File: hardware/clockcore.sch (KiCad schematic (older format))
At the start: 59 parts, among them J1 Header, J2 Ext, J3 JTAG, J7 GCT_USB4108-GF-A, Q1 MBT3904DW1T1G, SW1 Reset, SW2 Boot, U1 AP2114H-3_3TRG1, U2 ‎SN74HCT245PWR‎, U3 ESP32-WROOM-32, U4 DS1338Z-33+, U5 FT231XS, U6 USBLC6-4SC6, Y1 32.768Hz, 12.5pF, 45kΩ

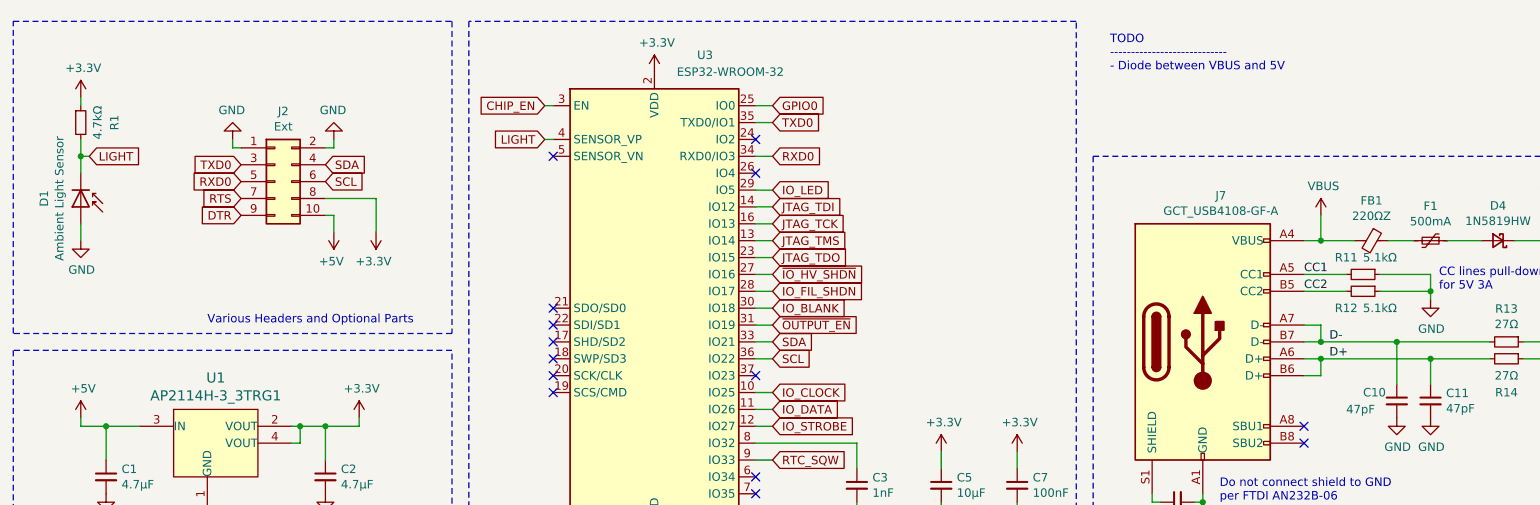
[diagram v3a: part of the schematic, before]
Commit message: add ds18b20 to clock core and reroute a few traces
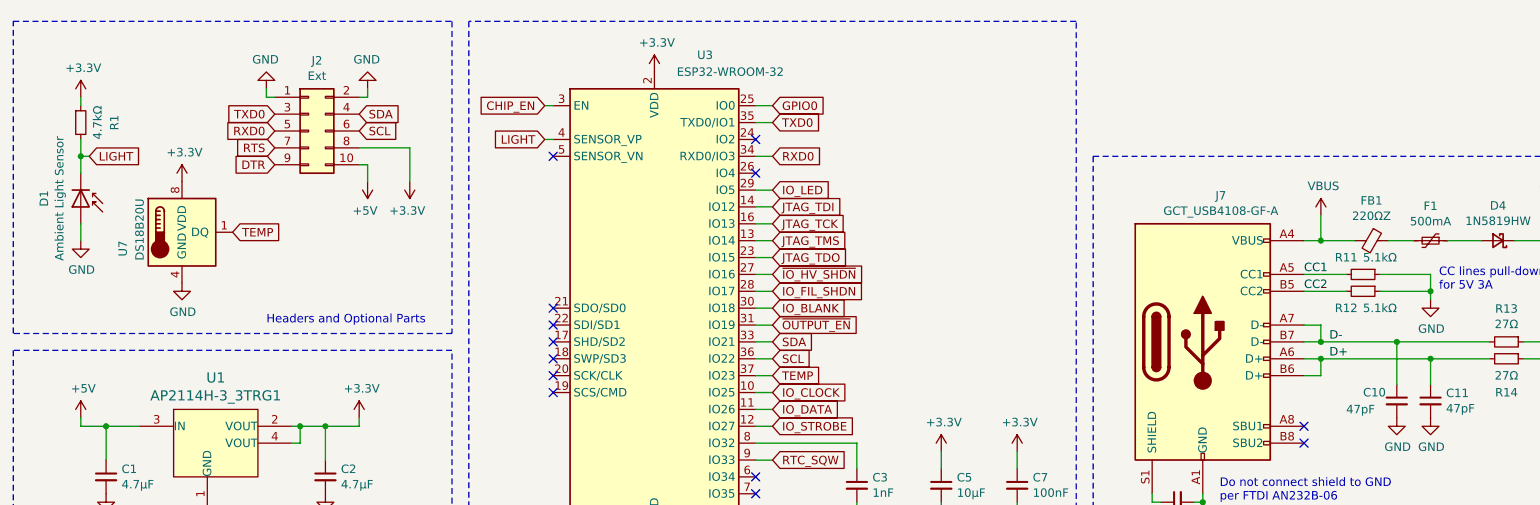
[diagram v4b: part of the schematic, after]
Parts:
- added U7: DS18B20U, Package_SO:MSOP-8_3x3mm_P0.65mm, symbol Sensor_Temperature:DS18B20U
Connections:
- net +3V3: now also U7.8 (VDD)
- net GND: now also U7.4 (GND)
- net TEMP: now reaches U3.37 (IO23)
- net TEMP: now also U7.1 (DQ)
- no-connect marks 27 -> 26
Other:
- note added: "Headers and Optional Parts"
- note removed: "TODO\n----------------------------\n- Diode between VBUS and 5V"
- note removed: "Various Headers and Optional Parts"
- moved on the sheet: J2
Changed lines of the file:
@@
 encoding utf-8
 Sheet 1 1
-Title ""
-Date ""
-Rev "1"
+Title "Clock Core"
+Date "2020-08-02"
+Rev "1.0"
 Comp ""
 Comment1 "Designed for AISLER 2-Layer Service"
-Comment2 ""
-Comment3 ""
+Comment2 "Made for IVL2-7/5 VFD Driver Board"
+Comment3 "ESP32 + RTC"
 Comment4 ""
 $EndDescr
@@
 L power:GND #PWR03
 U 1 1 5F700789
-P 2450 1300
-F 0 "#PWR03" H 2450 1050 50  0001 C CNN
-F 1 "GND" H 2455 1127 50  0000 C CNN
-F 2 "" H 2450 1300 50  0001 C CNN
-F 3 "" H 2450 1300 50  0001 C CNN
-	1    2450 1300
+P 2650 1000
+F 0 "#PWR03" H 2650 750 50  0001 C CNN
+F 1 "GND" H 2655 827 50  0000 C CNN
+F 2 "" H 2650 1000 50  0001 C CNN
+F 3 "" H 2650 1000 50  0001 C CNN
+	1    2650 1000
 	-1   0    0    1
 $EndComp
@@
 L power:GND #PWR010
 U 1 1 5F700DB1
-P 1850 1300
-F 0 "#PWR010" H 1850 1050 50  0001 C CNN
-F 1 "GND" H 1855 1127 50  0000 C CNN
-F 2 "" H 1850 1300 50  0001 C CNN
-F 3 "" H 1850 1300 50  0001 C CNN
-	1    1850 1300
+P 2050 1000
+F 0 "#PWR010" H 2050 750 50  0001 C CNN
+F 1 "GND" H 2055 827 50  0000 C CNN
+F 2 "" H 2050 1000 50  0001 C CNN
+F 3 "" H 2050 1000 50  0001 C CNN
+	1    2050 1000
 	-1   0    0    1
 $EndComp
@@
 L power:+3.3V #PWR02
 U 1 1 5F713013
-P 2700 1850
-F 0 "#PWR02" H 2700 1700 50  0001 C CNN
-F 1 "+3.3V" H 2715 2023 50  0000 C CNN
-F 2 "" H 2700 1850 50  0001 C CNN
-F 3 "" H 2700 1850 50  0001 C CNN
-	1    2700 1850
+P 2900 1550
+F 0 "#PWR02" H 2900 1400 50  0001 C CNN
+F 1 "+3.3V" H 2915 1723 50  0000 C CNN
+F 2 "" H 2900 1550 50  0001 C CNN
+F 3 "" H 2900 1550 50  0001 C CNN
+	1    2900 1550
 	-1   0    0    1
 $EndComp
@@
 L power:+5V #PWR08
 U 1 1 5F713FBF
-P 2450 1850
-F 0 "#PWR08" H 2450 1700 50  0001 C CNN
-F 1 "+5V" H 2465 2023 50  0000 C CNN
-F 2 "" H 2450 1850 50  0001 C CNN
-F 3 "" H 2450 1850 50  0001 C CNN
-	1    2450 1850
+P 2650 1550
+F 0 "#PWR08" H 2650 1400 50  0001 C CNN
+F 1 "+5V" H 2665 1723 50  0000 C CNN
+F 2 "" H 2650 1550 50  0001 C CNN
+F 3 "" H 2650 1550 50  0001 C CNN
+	1    2650 1550
 	-1   0    0    1
 $EndComp
-Text GLabel 2400 1450 2    50   Input ~ 0
+Text GLabel 2600 1150 2    50   Input ~ 0
 SDA
-Text GLabel 2400 1550 2    50   Input ~ 0
+Text GLabel 2600 1250 2    50   Input ~ 0
 SCL
-Text GLabel 1900 1450 0    50   Input ~ 0
+Text GLabel 2100 1150 0    50   Input ~ 0
 TXD0
-Text GLabel 1900 1550 0    50   Input ~ 0
+Text GLabel 2100 1250 0    50   Input ~ 0
 RXD0
-Text GLabel 1900 1650 0    50   Input ~ 0
+Text GLabel 2100 1350 0    50   Input ~ 0
 RTS
-Text GLabel 1900 1750 0    50   Input ~ 0
+Text GLabel 2100 1450 0    50   Input ~ 0
 DTR
 $Comp
@@
 Wire Notes Line
 	3150 2450 550  2450
-Text Notes 1700 2400 0    50   ~ 0
-Various Headers and Optional Parts
+Text Notes 2050 2400 0    50   ~ 0
+Headers and Optional Parts
 Text GLabel 5050 1100 2    50   Input ~ 0
 GPIO0
@@
 Wire Wire Line
 	4950 2400 5050 2400
-NoConn ~ 4950 2700
 Wire Notes Line
 	3250 600  3250 4000
@@
 NoConn ~ 1200 5350
 Wire Wire Line
-	2450 1300 2450 1350
-Wire Wire Line
-	2450 1350 2400 1350
-Wire Wire Line
-	1900 1350 1850 1350
-Wire Wire Line
-	1850 1350 1850 1300
-Wire Wire Line
-	2400 1750 2450 1750
-Wire Wire Line
-	2450 1750 2450 1850
-Wire Wire Line
-	2400 1650 2700 1650
-Wire Wire Line
-	2700 1650 2700 1850
+	2650 1000 2650 1050
+Wire Wire Line
+	2650 1050 2600 1050
+Wire Wire Line
+	2100 1050 2050 1050
+Wire Wire Line
+	2050 1050 2050 1000
+Wire Wire Line
+	2600 1450 2650 1450
+Wire Wire Line
+	2650 1450 2650 1550
+Wire Wire Line
+	2600 1350 2900 1350
+Wire Wire Line
+	2900 1350 2900 1550
 $Comp
 L Connector_Generic:Conn_02x05_Odd_Even J2
 U 1 1 5F5E992B
-P 2100 1550
-F 0 "J2" H 2150 1967 50  0000 C CNN
-F 1 "Ext" H 2150 1876 50  0000 C CNN
-F 2 "Connector_PinHeader_2.54mm:PinHeader_2x05_P2.54mm_Vertical" H 2100 1550 50  0001 C CNN
-F 3 "~" H 2100 1550 50  0001 C CNN
-	1    2100 1550
+P 2300 1250
+F 0 "J2" H 2350 1667 50  0000 C CNN
+F 1 "Ext" H 2350 1576 50  0000 C CNN
+F 2 "Connector_PinHeader_2.54mm:PinHeader_2x05_P2.54mm_Vertical" H 2300 1250 50  0001 C CNN
+F 3 "~" H 2300 1250 50  0001 C CNN
+	1    2300 1250
 	1    0    0    -1
 $EndComp
@@
 	1    0    0    -1
 $EndComp
-Text Notes 7050 900  0    50   ~ 0
-TODO\n----------------------------\n- Diode between VBUS and 5V
 Wire Wire Line
 	8500 1900 8300 1900
@@
 Wire Wire Line
 	9450 1900 9650 1900
+$Comp
+L Sensor_Temperature:DS18B20U U7
+U 1 1 5F27C2CD
+P 1550 1850
+F 0 "U7" V 1200 1800 50  0000 R CNN
+F 1 "DS18B20U" V 1300 2050 50  0000 R CNN
+F 2 "Package_SO:MSOP-8_3x3mm_P0.65mm" H 600 1600 50  0001 C CNN
+F 3 "http://datasheets.maximintegrated.com/en/ds/DS18B20.pdf" H 1400 2100 50  0001 C CNN
+	1    1550 1850
+	1    0    0    -1
+$EndComp
+$Comp
+L power:+3.3V #PWR0101
+U 1 1 5F27DD47
+P 1550 1550
+F 0 "#PWR0101" H 1550 1400 50  0001 C CNN
+F 1 "+3.3V" H 1565 1723 50  0000 C CNN
+F 2 "" H 1550 1550 50  0001 C CNN
+F 3 "" H 1550 1550 50  0001 C CNN
+	1    1550 1550
+	1    0    0    -1
+$EndComp
+$Comp
+L power:GND #PWR0102
+U 1 1 5F27E074
+P 1550 2150
+F 0 "#PWR0102" H 1550 1900 50  0001 C CNN
+F 1 "GND" H 1555 1977 50  0000 C CNN
+F 2 "" H 1550 2150 50  0001 C CNN
+F 3 "" H 1550 2150 50  0001 C CNN
+	1    1550 2150
+	1    0    0    -1
+$EndComp
+Text GLabel 1850 1850 2    50   Input ~ 0
+TEMP
+Text GLabel 5050 2700 2    50   Input ~ 0
+TEMP
+Wire Wire Line
+	4950 2700 5050 2700
 $EndSCHEMATC

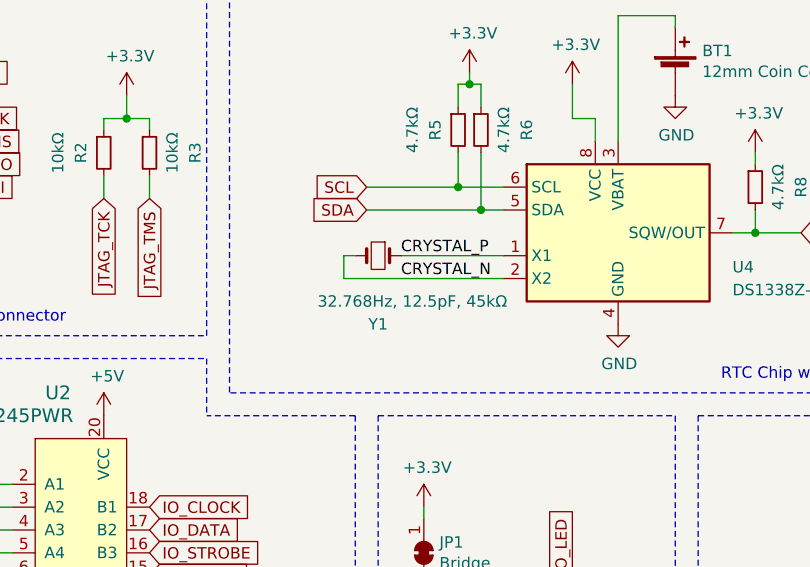
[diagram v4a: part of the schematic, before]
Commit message: updated crystal in schematic so pin3 is gnd, added teardrops
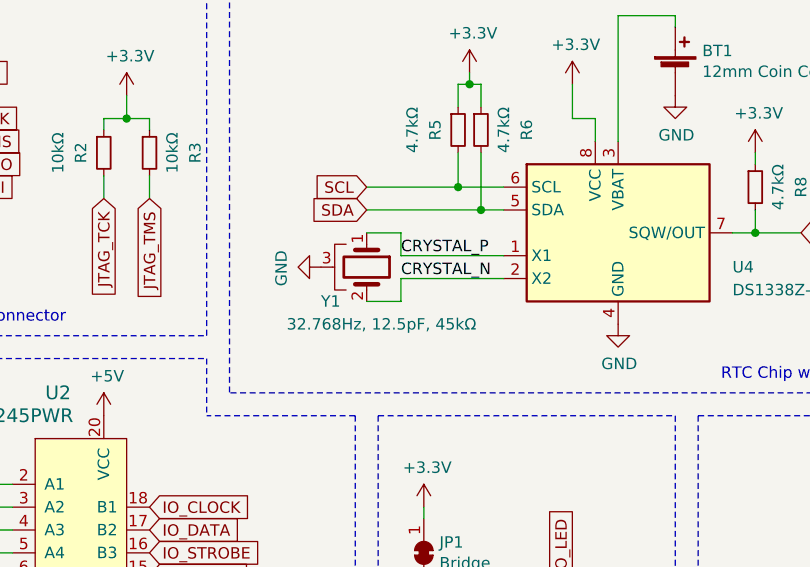
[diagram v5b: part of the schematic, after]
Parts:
- removed Y1: 32.768Hz, 12.5pF, 45kΩ, Crystal:Crystal_SMD_MicroCrystal_MS1V-T1K, symbol Device:Crystal_Small
- added Y1: 32.768Hz, 12.5pF, 45kΩ, Crystal:Crystal_SMD_MicroCrystal_MS1V-T1K, symbol Device:Crystal_GND3
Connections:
- net CRYSTAL_N: now also Y1.2
- net CRYSTAL_P: now also Y1.1
- net GND: now also Y1.3
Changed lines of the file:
@@
 Text GLabel 3850 4950 0    50   Input ~ 0
 SCL
-$Comp
-L Device:Crystal_Small Y1
-U 1 1 5F1C482B
-P 3900 5250
-F 0 "Y1" H 3900 5550 50  0000 C CNN
-F 1 "32.768Hz, 12.5pF, 45kΩ" H 3750 5450 50  0000 C CNN
-F 2 "Crystal:Crystal_SMD_MicroCrystal_MS1V-T1K" H 3900 5250 50  0001 C CNN
-F 3 "https://ecsxtal.com/store/pdf/ecs-2x6-flxr.pdf" H 3900 5250 50  0001 C CNN
-	1    3900 5250
-	-1   0    0    1
-$EndComp
-Wire Wire Line
-	3750 5350 3750 5250
-Wire Wire Line
-	3750 5250 3800 5250
 Text Label 4000 5250 0    50   ~ 0
 CRYSTAL_P
@@
 Wire Notes Line
 	6850 5850 3250 5850
-Wire Wire Line
-	3750 5350 4450 5350
-Wire Wire Line
-	4000 5250 4450 5250
 $Comp
 L Timer_RTC:DS1307ZN+ U4
@@
 Wire Wire Line
 	4950 2700 5050 2700
+$Comp
+L Device:Crystal_GND3 Y1
+U 1 1 5F35C657
+P 3850 5300
+F 0 "Y1" V 4000 5100 50  0000 L CNN
+F 1 "32.768Hz, 12.5pF, 45kΩ" V 4100 4950 50  0000 L CNN
+F 2 "Crystal:Crystal_SMD_MicroCrystal_MS1V-T1K" H 3850 5300 50  0001 C CNN
+F 3 "https://ecsxtal.com/store/pdf/ecs-2x6-flxr.pdf" H 3850 5300 50  0001 C CNN
+	1    3850 5300
+	0    1    1    0
+$EndComp
+Wire Wire Line
+	4000 5250 4450 5250
+Wire Wire Line
+	3850 5150 4000 5150
+Wire Wire Line
+	4000 5150 4000 5250
+Wire Wire Line
+	3850 5450 4000 5450
+Wire Wire Line
+	4000 5450 4000 5350
+Wire Wire Line
+	4000 5350 4450 5350
+$Comp
+L power:GND #PWR?
+U 1 1 5F38FE2E
+P 3650 5300
+F 0 "#PWR?" H 3650 5050 50  0001 C CNN
+F 1 "GND" H 3655 5127 50  0000 C CNN
+F 2 "" H 3650 5300 50  0001 C CNN
+F 3 "" H 3650 5300 50  0001 C CNN
+	1    3650 5300
+	0    1    1    0
+$EndComp
 $EndSCHEMATC

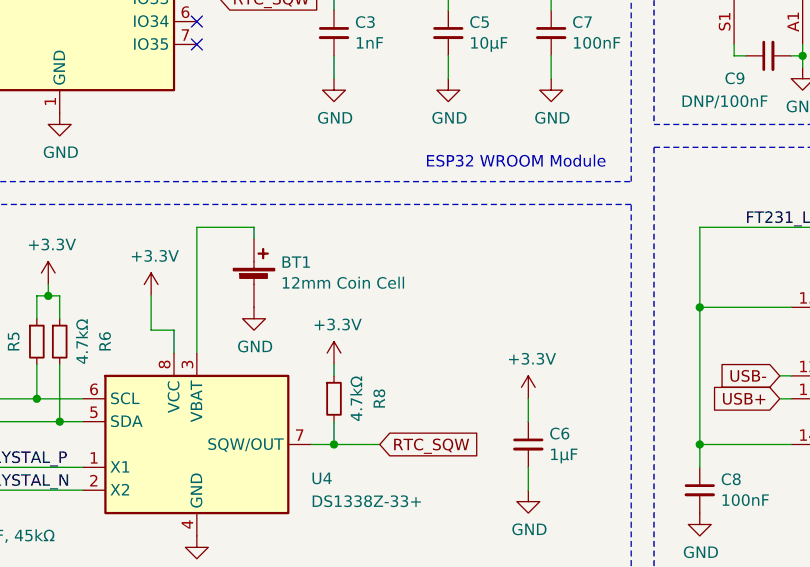
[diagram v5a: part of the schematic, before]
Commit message: add digikey bom for clockcore
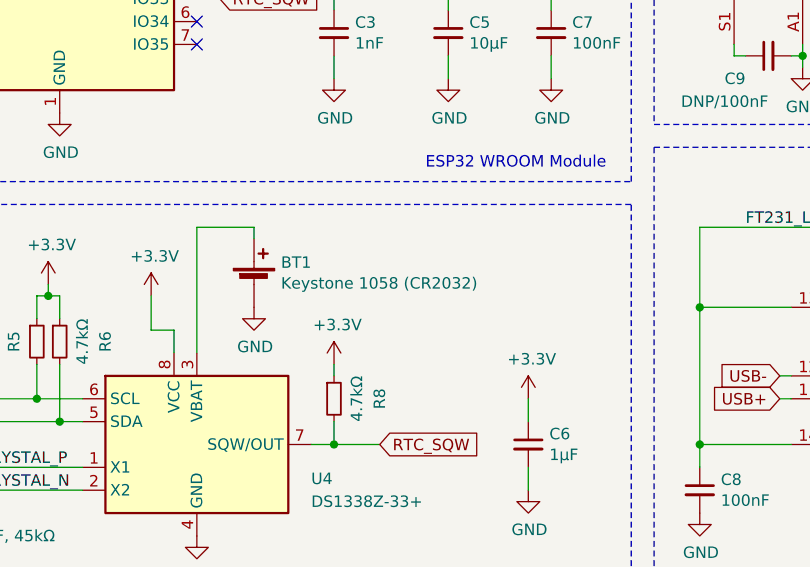
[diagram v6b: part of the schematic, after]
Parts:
- BT1: value 12mm Coin Cell -> Keystone 1058 (CR2032)
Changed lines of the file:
@@
 P 5200 4450
 F 0 "BT1" H 5318 4546 50  0000 L CNN
-F 1 "12mm Coin Cell" H 5318 4455 50  0000 L CNN
+F 1 "Keystone 1058 (CR2032)" H 5318 4455 50  0000 L CNN
 F 2 "Battery:BatteryHolder_Keystone_1058_1x2032" V 5200 4510 50  0001 C CNN
 F 3 "https://www.keyelco.com/userAssets/file/M65p9.pdf" V 5200 4510 50  0001 C CNN

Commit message: populate part numbers in clockcore symbol fields, generate new bom with kibom
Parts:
- BT1: Digi-Key_PN (none) -> 36-1058-ND; MPN (none) -> 1058; Manufacturer (none) -> Keystone
- C1, C15, C2: Digi-Key_PN (none) -> 1276-1244-1-ND; MPN (none) -> CL21A475KAQNNNE; Manufacturer (none) -> Samsung
- C10, C11: Digi-Key_PN (none) -> 311-1107-1-ND; MPN (none) -> CC0805JRNPO9BN470; Manufacturer (none) -> Yageo
- C12, C14, C4, C7, C8, C9: Digi-Key_PN (none) -> 1276-1099-1-ND; MPN (none) -> CL21B104KACNNNC; Manufacturer (none) -> Samsung
- C13: Digi-Key_PN (none) -> 311-1136-1-ND; MPN (none) -> CC0805KRX7R9BB103; Manufacturer (none) -> Yageo
- C3: Digi-Key_PN (none) -> 1276-1020-1-ND; MPN (none) -> CL21B102KBANNNC; Manufacturer (none) -> Samsung
- C5: Digi-Key_PN (none) -> 1276-1096-1-ND; MPN (none) -> CL21A106KOQNNNE; Manufacturer (none) -> Samsung
- C6: Digi-Key_PN (none) -> 1276-6469-1-ND; MPN (none) -> CL21B105KAFNNNG; Manufacturer (none) -> Samsung
- D1: Digi-Key_PN (none) -> VEMD1060X01CT-ND; MPN (none) -> VEMD1060X01; Manufacturer (none) -> Vishay
- D2: Digi-Key_PN (none) -> 732-4985-1-ND; MPN (none) -> 150080SS75000; Manufacturer (none) -> Würth
- D3: Digi-Key_PN (none) -> 732-4986-1-ND; MPN (none) -> 150080VS75000; Manufacturer (none) -> Würth
- D4: Digi-Key_PN (none) -> 1N5819HW-FDICT-ND; MPN (none) -> 1N5819HW-7-F; Manufacturer (none) -> Diodes Inc.
- F1: Digi-Key_PN (none) -> 507-1802-1-ND; MPN (none) -> 0ZCJ0050FF2G; Manufacturer (none) -> Bel Fuse
- FB1: Digi-Key_PN (none) -> 490-16661-1-ND; MPN (none) -> BLM21PG221SZ1D; Manufacturer (none) -> Murata
- J1: Digi-Key_PN (none) -> S7006-ND; MPN (none) -> PPTC081LFBN-RC; Manufacturer (none) -> Sullins
- J2: Digi-Key_PN (none) -> S2011EC-40-ND; MPN (none) -> PRPC040DAAN-RC; Manufacturer (none) -> Sullins
- J3: Digi-Key_PN (none) -> 609-3695-6-ND; MPN (none) -> 20021121-00010C4LF; Manufacturer (none) -> Amphenol
- J7: Digi-Key_PN (none) -> 2073-USB4105-GF-ACT-ND; MPN (none) -> USB4105-GF-A; Manufacturer (none) -> GCT
- R1, R5, R6, R8: Digi-Key_PN (none) -> 311-4.70KCRCT-ND; MPN (none) -> RC0805FR-074K7L; Manufacturer (none) -> Yageo
- R10, R15, R16, R2, R3, R9: Digi-Key_PN (none) -> 311-10.0KCRCT-ND; MPN (none) -> RC0805FR-0710KL; Manufacturer (none) -> Yageo
- R11, R12: Digi-Key_PN (none) -> 311-5.1KARCT-ND; MPN (none) -> RC0805JR-075K1L; Manufacturer (none) -> Yageo
- R13, R14: Digi-Key_PN (none) -> 311-27.0CRCT-ND; MPN (none) -> RC0805FR-0727RL; Manufacturer (none) -> Yageo
- R4, R7: Digi-Key_PN (none) -> 311-1.00KCRCT-ND; MPN (none) -> RC0805FR-071KL; Manufacturer (none) -> Yageo
- SW1, SW2: Digi-Key_PN (none) -> CKN12221-1-ND; MPN (none) -> PTS526 SK15 SMTR2 LFS; Manufacturer (none) -> C&K
- U1: Manufacturer Diodes Incorporated -> Diodes Inc.
- U2: Digi-Key_PN 296-8404-1-ND‎ -> 296-8404-1-ND; MPN SN74LVC245AN -> SN74HCT245PWR
- U3: Digi-Key_PN (none) -> 1965-ESP32-WROOM-32E(8MBFLASH)CT-ND; MPN (none) -> ESP32-WROOM-32E (8MB); Manufacturer (none) -> Espressif
- U4: Digi-Key_PN (none) -> DS1338Z-33+T&RCT-ND; MPN (none) -> DS1338Z-33+T&R; Manufacturer (none) -> Maxim
- U5: Digi-Key_PN (none) -> 768-1129-1-ND; MPN (none) -> FT231XS-R; Manufacturer (none) -> FTDI
- U6: Digi-Key_PN (none) -> 497-4492-1-ND; MPN (none) -> USBLC6-4SC6; Manufacturer (none) -> ST Microelectronic
- U7: Digi-Key_PN (none) -> DS18B20U+T&RCT-ND; MPN (none) -> DS18B20U+T&R; Manufacturer (none) -> Maxim
- Y1: Digi-Key_PN (none) -> XC1911CT-ND; MPN (none) -> ECS-.327-12.5-13FLX-C; Manufacturer (none) -> ECS Inc.

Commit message: add clockcore schematic pdf
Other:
- note added: "TODO: forgot onewire pullup\nis internal enough?"
- note added: "TODO: properly match\nbrightness. PWR (red)\nis brighter"
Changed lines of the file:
@@
-$EndComp
-$Comp
-L Device:LED_Small D2
-U 1 1 5F2EBC41
-P 4100 6900
-F 0 "D2" V 4146 6830 50  0000 R CNN
-F 1 "PWR LED" V 4055 6830 50  0000 R CNN
-F 2 "LED_SMD:LED_0805_2012Metric_Pad1.15x1.40mm_HandSolder" V 4100 6900 50  0001 C CNN
-F 3 "~" V 4100 6900 50  0001 C CNN
-F 4 "732-4985-1-ND" H 4100 6900 50  0001 C CNN "Digi-Key_PN"
-F 5 "150080SS75000" H 4100 6900 50  0001 C CNN "MPN"
-F 6 "Würth" H 4100 6900 50  0001 C CNN "Manufacturer"
-	1    4100 6900
-	0    -1   -1   0
 $EndComp
 $Comp
@@
 	1    4700 7150
 	1    0    0    -1
-$EndComp
-$Comp
-L Device:LED_Small D3
-U 1 1 5F2FA06D
-P 4700 6900
-F 0 "D3" V 4746 6830 50  0000 R CNN
-F 1 "GPIO LED" V 4655 6830 50  0000 R CNN
-F 2 "LED_SMD:LED_0805_2012Metric_Pad1.15x1.40mm_HandSolder" V 4700 6900 50  0001 C CNN
-F 3 "~" V 4700 6900 50  0001 C CNN
-F 4 "732-4986-1-ND" H 4700 6900 50  0001 C CNN "Digi-Key_PN"
-F 5 "150080VS75000" H 4700 6900 50  0001 C CNN "MPN"
-F 6 "Würth" H 4700 6900 50  0001 C CNN "Manufacturer"
-	1    4700 6900
-	0    -1   -1   0
 $EndComp
 $Comp
@@
 	0    1    1    0
 $EndComp
+Text Notes 1850 2100 0    50   ~ 0
+TODO: forgot onewire pullup\nis internal enough?
+Text Notes 4300 6250 0    50   ~ 0
+TODO: properly match\nbrightness. PWR (red)\nis brighter
+$Comp
+L Device:LED_Small D3
+U 1 1 5F2FA06D
+P 4700 6900
+F 0 "D3" V 4746 6830 50  0000 R CNN
+F 1 "GPIO LED" V 4655 6830 50  0000 R CNN
+F 2 "LED_SMD:LED_0805_2012Metric_Pad1.15x1.40mm_HandSolder" V 4700 6900 50  0001 C CNN
+F 3 "~" V 4700 6900 50  0001 C CNN
+F 4 "732-4986-1-ND" H 4700 6900 50  0001 C CNN "Digi-Key_PN"
+F 5 "150080VS75000" H 4700 6900 50  0001 C CNN "MPN"
+F 6 "Würth" H 4700 6900 50  0001 C CNN "Manufacturer"
+	1    4700 6900
+	0    -1   -1   0
+$EndComp
+$Comp
+L Device:LED_Small D2
+U 1 1 5F2EBC41
+P 4100 6900
+F 0 "D2" V 4146 6830 50  0000 R CNN
+F 1 "PWR LED" V 4055 6830 50  0000 R CNN
+F 2 "LED_SMD:LED_0805_2012Metric_Pad1.15x1.40mm_HandSolder" V 4100 6900 50  0001 C CNN
+F 3 "~" V 4100 6900 50  0001 C CNN
+F 4 "732-4985-1-ND" H 4100 6900 50  0001 C CNN "Digi-Key_PN"
+F 5 "150080SS75000" H 4100 6900 50  0001 C CNN "MPN"
+F 6 "Würth" H 4100 6900 50  0001 C CNN "Manufacturer"
+	1    4100 6900
+	0    -1   -1   0
+$EndComp
 $EndSCHEMATC
